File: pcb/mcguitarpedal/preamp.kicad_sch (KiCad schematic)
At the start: 26 parts, among them J8 POT_HP_VOLUME_10k, U3 LM4562

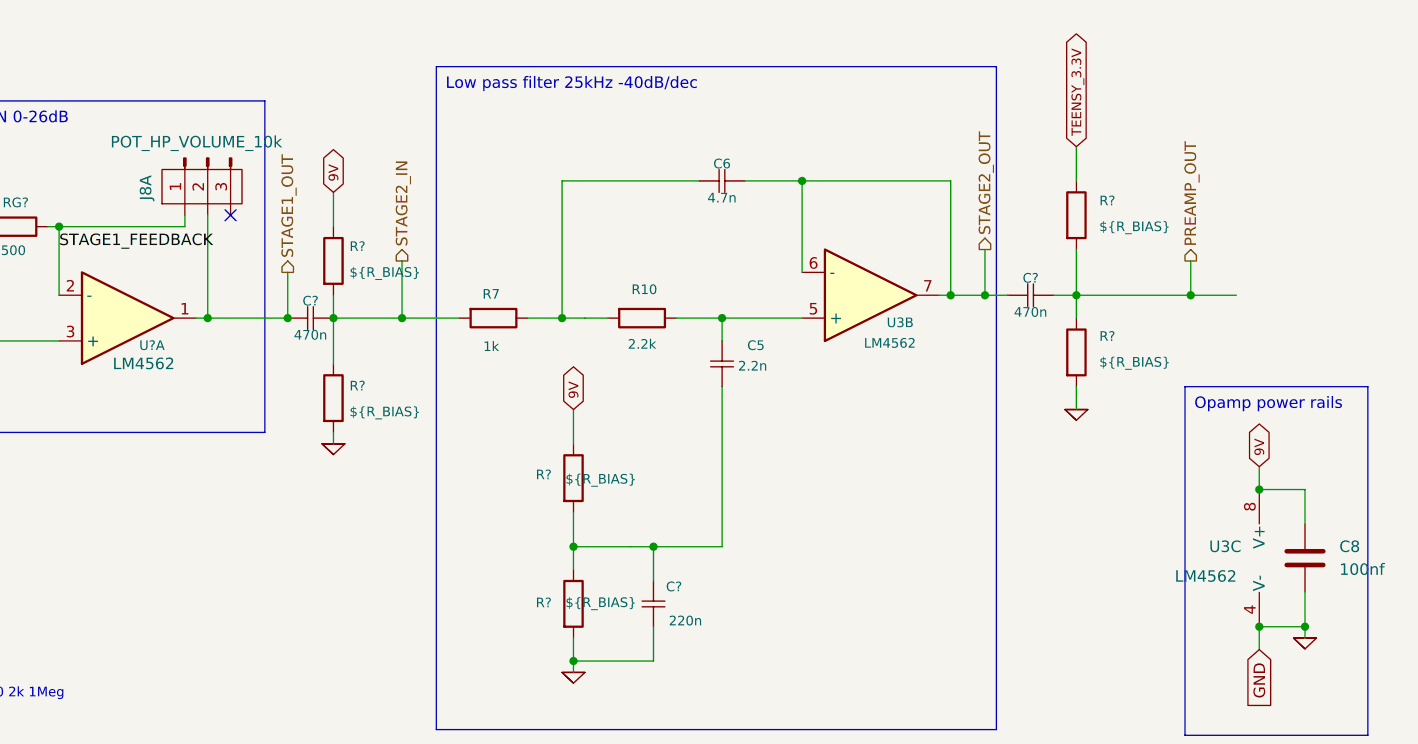
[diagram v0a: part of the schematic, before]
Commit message: Rearranged pullups
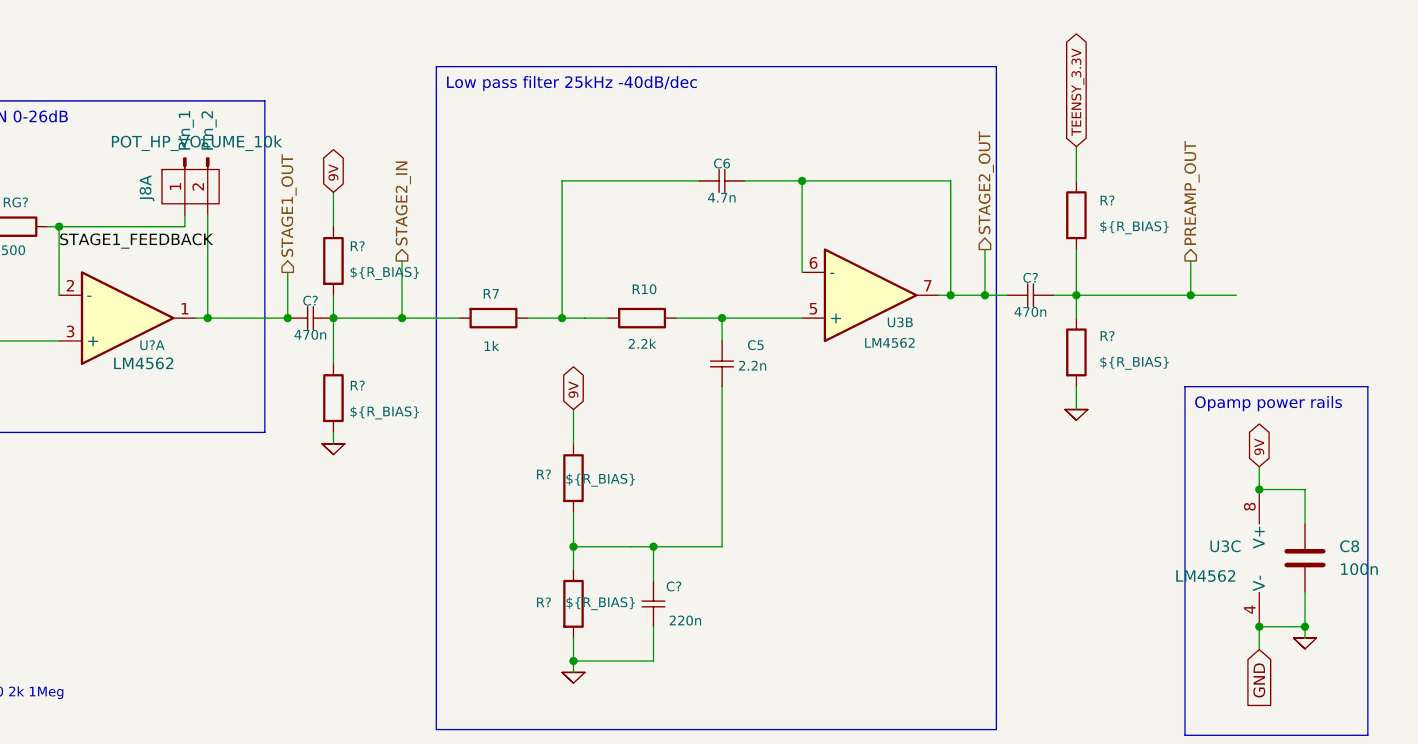
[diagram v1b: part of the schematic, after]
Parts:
- C8: value 100nf -> 100n
- J8: footprint Connector_PinHeader_2.54mm:PinHeader_1x09_P2.54mm_Vertical -> mcguitarpedal:POTS_HEADER
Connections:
- no-connect marks 1 -> 0
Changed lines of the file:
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@@
 		(color 0 0 0 0)
 	)
-	(no_connect
-		(at 119.38 90.17)
-	)
 	(wire
 		(pts
@@
 			)
 		)
-		(property "Value" "100nf"
+		(property "Value" "100n"
 			(at 242.57 129.5399 0)
 			(effects
@@
 			)
 		)
-		(property "Footprint" "Connector_PinHeader_2.54mm:PinHeader_1x09_P2.54mm_Vertical"
+		(property "Footprint" "mcguitarpedal:POTS_HEADER"
 			(at 115.57 83.82 0)
 			(effects
@@
 		(pin "4"
 		)
-		(pin "3"
-		)
 		(pin "2"

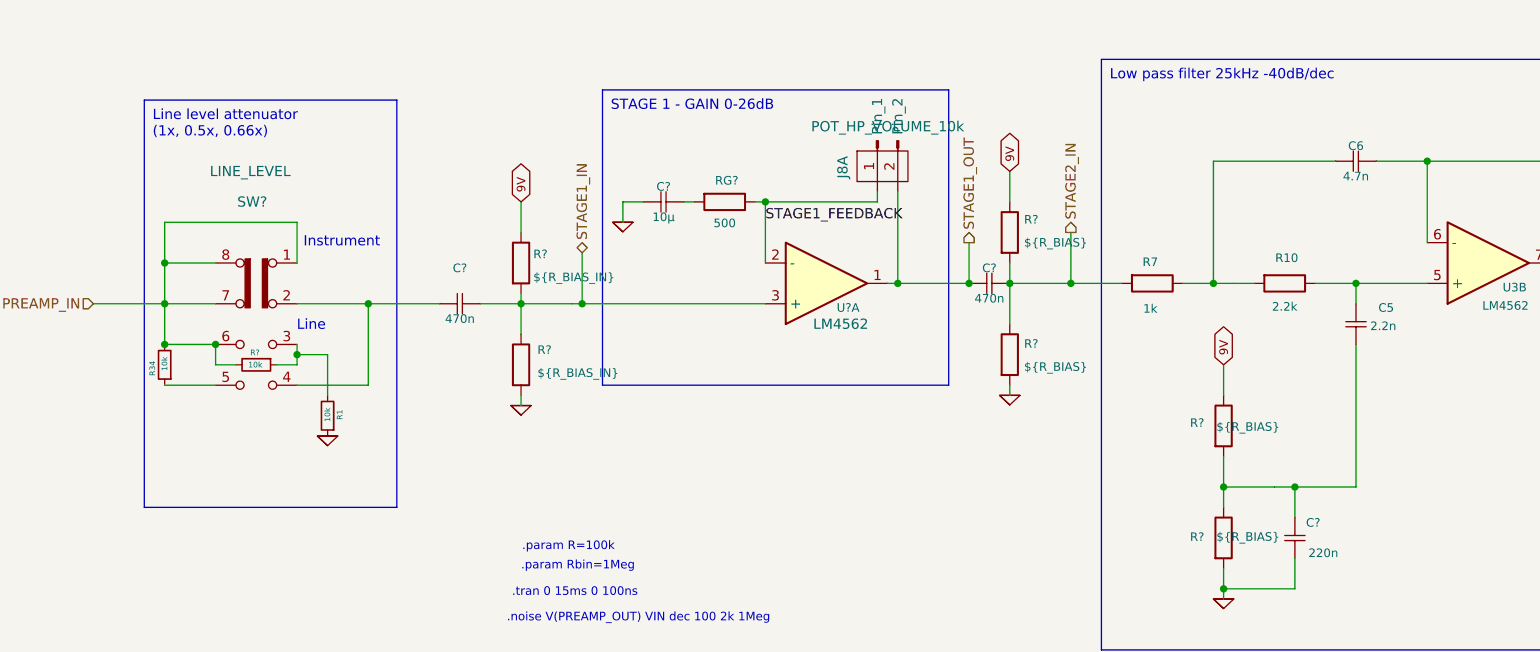
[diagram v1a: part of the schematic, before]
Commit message: Silkscreen labeling
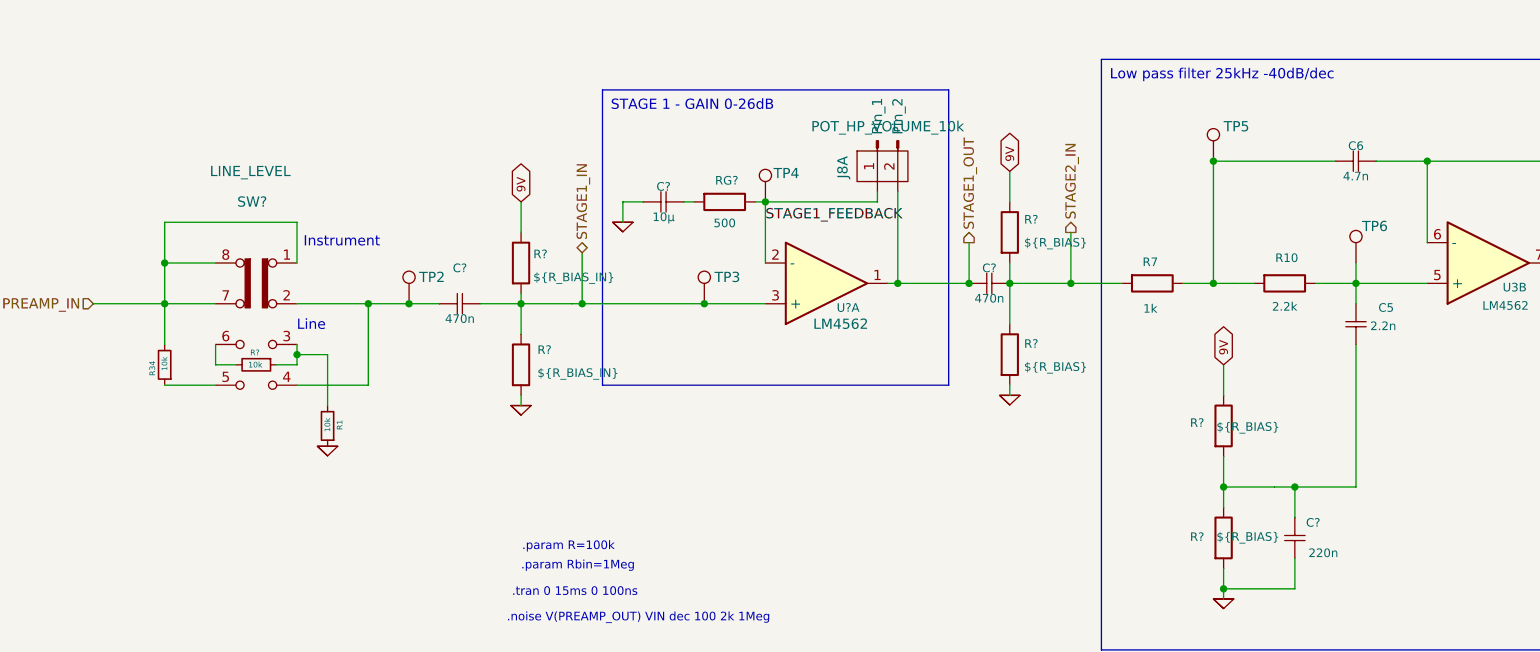
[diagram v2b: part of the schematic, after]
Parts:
- added TP2, TP3, TP4, TP5, TP6: TestPoint, TestPoint:TestPoint_Loop_D1.80mm_Drill1.0mm_Beaded, symbol Connector:TestPoint
- C8: footprint Capacitor_THT:C_Rect_L7.2mm_W2.5mm_P5.00mm_FKS2_FKP2_MKS2_MKP2 -> Capacitor_SMD:C_1206_3216Metric_Pad1.33x1.80mm_HandSolder
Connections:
- net PREAMP_IN: no longer R?.2, SW?.6 (A)
- net STAGE1_FEEDBACK: now also TP4.1
- net STAGE1_IN: now also TP3.1
- net at C6.2, R10.2, R7.1: now also TP5.1
- net at C5.1, R10.1, U3.5 (+): now also TP6.1
- net at C?.2, SW?.2 (B), SW?.4 (D): now also TP2.1
- new net: R?.2, SW?.6 (A)
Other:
- moved on the sheet: R1

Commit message: Final 1.0 design
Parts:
- U3, U?: footprint LM4562:lm4562 -> TI_FOOTPRINTS:lm4562
- renumbered C5 to C14, C6 to C15, C8 to C17, R34 to R30, R1 to R32, R7 to R37, R10 to R40, TP4 to TP10, TP5 to TP11, TP6 to TP12, TP2 to TP8, TP3 to TP9
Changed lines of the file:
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@@
 		(on_board yes)
 		(dnp no)
-		(property "Reference" "R7"
+		(property "Reference" "R37"
 			(at 148.336 99.568 90)
 			(effects
@@
 			(project "mcguitarpedal"
 				(path "/abf63e65-3dbc-486e-8cbe-833bb40c3c0d/c177d22b-45a9-4502-a618-667d0401078d"
-					(reference "R7")
+					(reference "R37")
 					(unit 1)
 				)
@@
 			(project "mcguitarpedal"
 				(path "/abf63e65-3dbc-486e-8cbe-833bb40c3c0d/c177d22b-45a9-4502-a618-667d0401078d"
-					(reference "R4")
+					(reference "R34")
 					(unit 1)
 				)
@@
 		(on_board yes)
 		(dnp no)
-		(property "Reference" "#GND03"
+		(property "Reference" "#GND01"
 			(at 45.72 121.92 0)
 			(effects
@@
 			(project "mcguitarpedal"
 				(path "/abf63e65-3dbc-486e-8cbe-833bb40c3c0d/c177d22b-45a9-4502-a618-667d0401078d"
-					(reference "#GND03")
+					(reference "#GND01")
 					(unit 1)
 				)
@@
 		(on_board yes)
 		(dnp no)
-		(property "Reference" "C5"
+		(property "Reference" "C14"
 			(at 176.784 104.648 0)
 			(effects
@@
 			(project "mcguitarpedal"
 				(path "/abf63e65-3dbc-486e-8cbe-833bb40c3c0d/c177d22b-45a9-4502-a618-667d0401078d"
-					(reference "C5")
+					(reference "C14")
 					(unit 1)
 				)
@@
 		(on_board yes)
 		(dnp no)
-		(property "Reference" "TP2"
+		(property "Reference" "TP8"
 			(at 57.15 100.838 0)
 			(effects
@@
 			(project "mcguitarpedal"
 				(path "/abf63e65-3dbc-486e-8cbe-833bb40c3c0d/c177d22b-45a9-4502-a618-667d0401078d"
-					(reference "TP2")
+					(reference "TP8")
 					(unit 1)
 				)
@@
 		(on_board yes)
 		(dnp no)
-		(property "Reference" "C6"
+		(property "Reference" "C15"
 			(at 173.99 85.09 90)
 			(effects
@@
 			(project "mcguitarpedal"
 				(path "/abf63e65-3dbc-486e-8cbe-833bb40c3c0d/c177d22b-45a9-4502-a618-667d0401078d"
-					(reference "C6")
+					(reference "C15")
 					(unit 1)
 				)
@@
 			(project "mcguitarpedal"
 				(path "/abf63e65-3dbc-486e-8cbe-833bb40c3c0d/c177d22b-45a9-4502-a618-667d0401078d"
-					(reference "#GND010")
+					(reference "#GND03")
 					(unit 1)
 				)
@@
 			(project "mcguitarpedal"
 				(path "/abf63e65-3dbc-486e-8cbe-833bb40c3c0d/c177d22b-45a9-4502-a618-667d0401078d"
-					(reference "C4")
+					(reference "C13")
 					(unit 1)
 				)
@@
 				)
 				(path "/abf63e65-3dbc-486e-8cbe-833bb40c3c0d/c177d22b-45a9-4502-a618-667d0401078d"
-					(reference "SW4")
+					(reference "SW5")
 					(unit 1)
 				)
@@
 			(project "mcguitarpedal"
 				(path "/abf63e65-3dbc-486e-8cbe-833bb40c3c0d/c177d22b-45a9-4502-a618-667d0401078d"
-					(reference "C1")
+					(reference "C10")
 					(unit 1)
 				)
@@
 		(on_board yes)
 		(dnp no)
-		(property "Reference" "TP4"
+		(property "Reference" "TP10"
 			(at 101.346 87.884 0)
 			(effects
@@
 			(project "mcguitarpedal"
 				(path "/abf63e65-3dbc-486e-8cbe-833bb40c3c0d/c177d22b-45a9-4502-a618-667d0401078d"
-					(reference "TP4")
+					(reference "TP10")
 					(unit 1)
 				)
@@
 			)
 		)
-		(property "Footprint" "LM4562:lm4562"
+		(property "Footprint" "TI_FOOTPRINTS:lm4562"
 			(at 236.22 128.27 0)
 			(effects
@@
 			(project "mcguitarpedal"
 				(path "/abf63e65-3dbc-486e-8cbe-833bb40c3c0d/c177d22b-45a9-4502-a618-667d0401078d"
-					(reference "C2")
+					(reference "C11")
 					(unit 1)
 				)
@@
 			(project "mcguitarpedal"
 				(path "/abf63e65-3dbc-486e-8cbe-833bb40c3c0d/c177d22b-45a9-4502-a618-667d0401078d"
-					(reference "#GND09")
+					(reference "#GND02")
 					(unit 1)
 				)
@@
 		(on_board yes)
 		(dnp no)
-		(property "Reference" "R34"
+		(property "Reference" "R30"
 			(at 23.876 111.252 90)
 			(effects
@@
 			(project "mcguitarpedal"
 				(path "/abf63e65-3dbc-486e-8cbe-833bb40c3c0d/c177d22b-45a9-4502-a618-667d0401078d"
-					(reference "R34")
+					(reference "R30")
 					(unit 1)
 				)
@@
 			(project "mcguitarpedal"
 				(path "/abf63e65-3dbc-486e-8cbe-833bb40c3c0d/c177d22b-45a9-4502-a618-667d0401078d"
-					(reference "#GND013")
+					(reference "#GND06")
 					(unit 1)
 				)
@@
 		(on_board yes)
 		(dnp no)
-		(property "Reference" "C8"
+		(property "Reference" "C17"
 			(at 242.57 126.9999 0)
 			(effects
@@
 			(project ""
 				(path "/abf63e65-3dbc-486e-8cbe-833bb40c3c0d/c177d22b-45a9-4502-a618-667d0401078d"
-					(reference "C8")
+					(reference "C17")
 					(unit 1)
 				)
@@
 			(project "mcguitarpedal"
 				(path "/abf63e65-3dbc-486e-8cbe-833bb40c3c0d/c177d22b-45a9-4502-a618-667d0401078d"
-					(reference "R11")
+					(reference "R41")
 					(unit 1)
 				)
@@
 		(on_board yes)
 		(dnp no)
-		(property "Reference" "R1"
+		(property "Reference" "R32"
 			(at 47.244 118.618 90)
 			(effects
@@
 			(project "mcguitarpedal"
 				(path "/abf63e65-3dbc-486e-8cbe-833bb40c3c0d/c177d22b-45a9-4502-a618-667d0401078d"
-					(reference "R1")
+					(reference "R32")
 					(unit 1)
 				)
@@
 			(project "mcguitarpedal"
 				(path "/abf63e65-3dbc-486e-8cbe-833bb40c3c0d/c177d22b-45a9-4502-a618-667d0401078d"
-					(reference "R8")
+					(reference "R38")
 					(unit 1)
 				)
@@
 			)
 		)
-		(property "Footprint" "LM4562:lm4562"
+		(property "Footprint" "TI_FOOTPRINTS:lm4562"
 			(at 107.95 101.6 0)
 			(effects
@@
 			(project "mcguitarpedal"
 				(path "/abf63e65-3dbc-486e-8cbe-833bb40c3c0d/c177d22b-45a9-4502-a618-667d0401078d"
-					(reference "R5")
+					(reference "R35")
 					(unit 1)
 				)
@@
 		(on_board yes)
 		(dnp no)
-		(property "Reference" "R10"
+		(property "Reference" "R40"
 			(at 165.354 99.06 90)
 			(effects
@@
 			(project "mcguitarpedal"
 				(path "/abf63e65-3dbc-486e-8cbe-833bb40c3c0d/c177d22b-45a9-4502-a618-667d0401078d"
-					(reference "R10")
+					(reference "R40")
 					(unit 1)
 				)
@@
 		(on_board yes)
 		(dnp no)
-		(property "Reference" "TP5"
+		(property "Reference" "TP11"
 			(at 157.48 82.042 0)
 			(effects
@@
 			(project "mcguitarpedal"
 				(path "/abf63e65-3dbc-486e-8cbe-833bb40c3c0d/c177d22b-45a9-4502-a618-667d0401078d"
-					(reference "TP5")
+					(reference "TP11")
 					(unit 1)
 				)
@@
 			(project "mcguitarpedal"
 				(path "/abf63e65-3dbc-486e-8cbe-833bb40c3c0d/c177d22b-45a9-4502-a618-667d0401078d"
-					(reference "R6")
+					(reference "R36")
 					(unit 1)
 				)
@@
 		(on_board yes)
 		(dnp no)
-		(property "Reference" "#GND01"
+		(property "Reference" "#GND07"
 			(at 238.76 137.16 0)
 			(effects
@@
 			(project "mcguitarpedal"
 				(path "/abf63e65-3dbc-486e-8cbe-833bb40c3c0d/c177d22b-45a9-4502-a618-667d0401078d"
-					(reference "#GND01")
+					(reference "#GND07")
 					(unit 1)
 				)
@@
 			(project "mcguitarpedal"
 				(path "/abf63e65-3dbc-486e-8cbe-833bb40c3c0d/c177d22b-45a9-4502-a618-667d0401078d"
-					(reference "#GND011")
+					(reference "#GND04")
 					(unit 1)
 				)
@@
 			(project "mcguitarpedal"
 				(path "/abf63e65-3dbc-486e-8cbe-833bb40c3c0d/c177d22b-45a9-4502-a618-667d0401078d"
-					(reference "#GND012")
+					(reference "#GND05")
 					(unit 1)
 				)
@@
 			(project "mcguitarpedal"
 				(path "/abf63e65-3dbc-486e-8cbe-833bb40c3c0d/c177d22b-45a9-4502-a618-667d0401078d"
-					(reference "R12")
+					(reference "R42")
 					(unit 1)
 				)
@@
 			(project "mcguitarpedal"
 				(path "/abf63e65-3dbc-486e-8cbe-833bb40c3c0d/c177d22b-45a9-4502-a618-667d0401078d"
-					(reference "C3")
+					(reference "C12")
 					(unit 1)
 				)
@@
 			(project "mcguitarpedal"
 				(path "/abf63e65-3dbc-486e-8cbe-833bb40c3c0d/c177d22b-45a9-4502-a618-667d0401078d"
-					(reference "R3")
+					(reference "R33")
 					(unit 1)
 				)
@@
 		(on_board yes)
 		(dnp no)
-		(property "Reference" "TP6"
+		(property "Reference" "TP12"
 			(at 174.752 94.488 0)
 			(effects
@@
 			(project ""
 				(path "/abf63e65-3dbc-486e-8cbe-833bb40c3c0d/c177d22b-45a9-4502-a618-667d0401078d"
-					(reference "TP6")
+					(reference "TP12")
 					(unit 1)
 				)
@@
 			)
 		)
-		(property "Footprint" "LM4562:lm4562"
+		(property "Footprint" "TI_FOOTPRINTS:lm4562"
 			(at 190.5 99.06 0)
 			(effects
@@
 			(project "mcguitarpedal"
 				(path "/abf63e65-3dbc-486e-8cbe-833bb40c3c0d/c177d22b-45a9-4502-a618-667d0401078d"
-					(reference "R2")
+					(reference "R31")
 					(unit 1)
 				)
@@
 		(on_board yes)
 		(dnp no)
-		(property "Reference" "TP3"
+		(property "Reference" "TP9"
 			(at 93.98 100.838 0)
 			(effects
@@
 			(project "mcguitarpedal"
 				(path "/abf63e65-3dbc-486e-8cbe-833bb40c3c0d/c177d22b-45a9-4502-a618-667d0401078d"
-					(reference "TP3")
+					(reference "TP9")
 					(unit 1)
 				)
@@
 			(project "mcguitarpedal"
 				(path "/abf63e65-3dbc-486e-8cbe-833bb40c3c0d/c177d22b-45a9-4502-a618-667d0401078d"
-					(reference "R9")
+					(reference "R39")
 					(unit 1)
 				)
@@
 			(project "mcguitarpedal"
 				(path "/abf63e65-3dbc-486e-8cbe-833bb40c3c0d/c177d22b-45a9-4502-a618-667d0401078d"
-					(reference "C7")
+					(reference "C16")
 					(unit 1)
 				)
